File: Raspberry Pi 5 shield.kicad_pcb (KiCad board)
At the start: 2 copper layers, 65 x 56 mm, 18 parts, among them J1 Raspberry Connector, J2 Conn_02x02_Odd_Even, U1 MCP2515-xSO

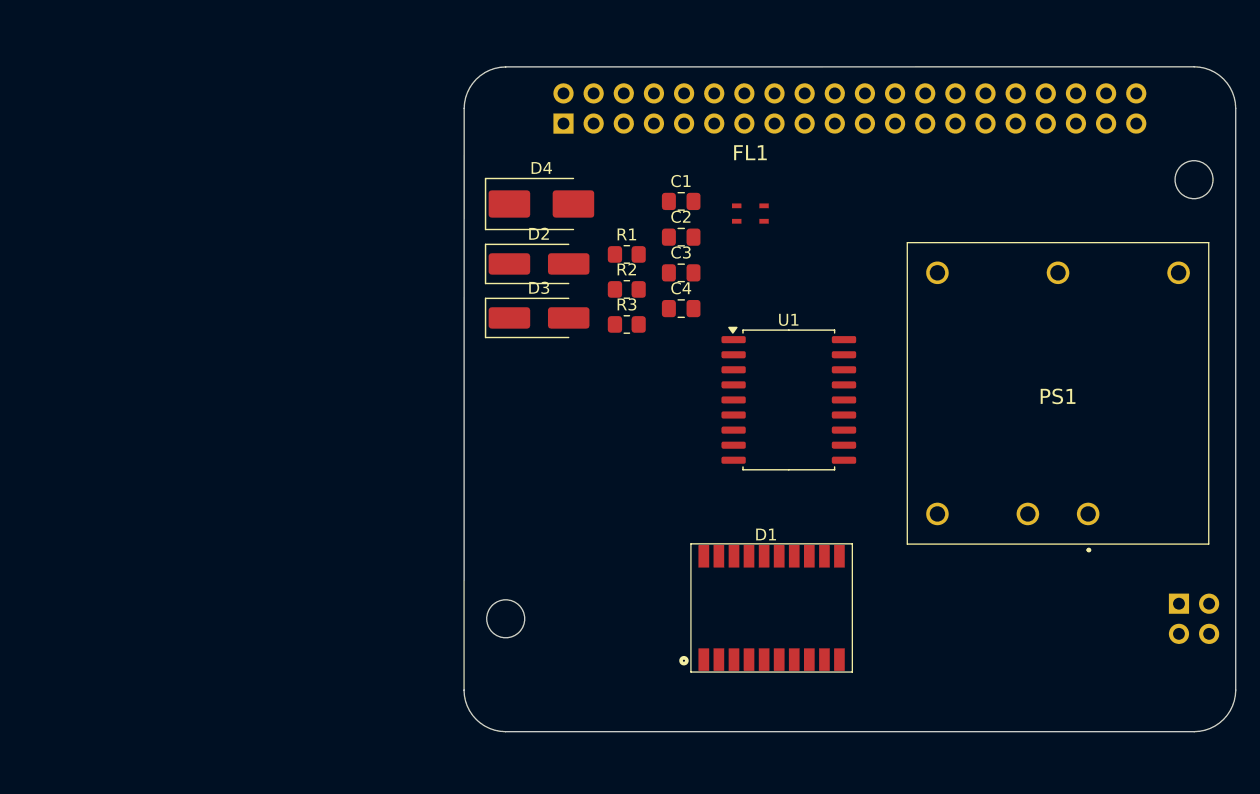
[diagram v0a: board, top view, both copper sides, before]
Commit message: Добавил конденсаторы по выходу
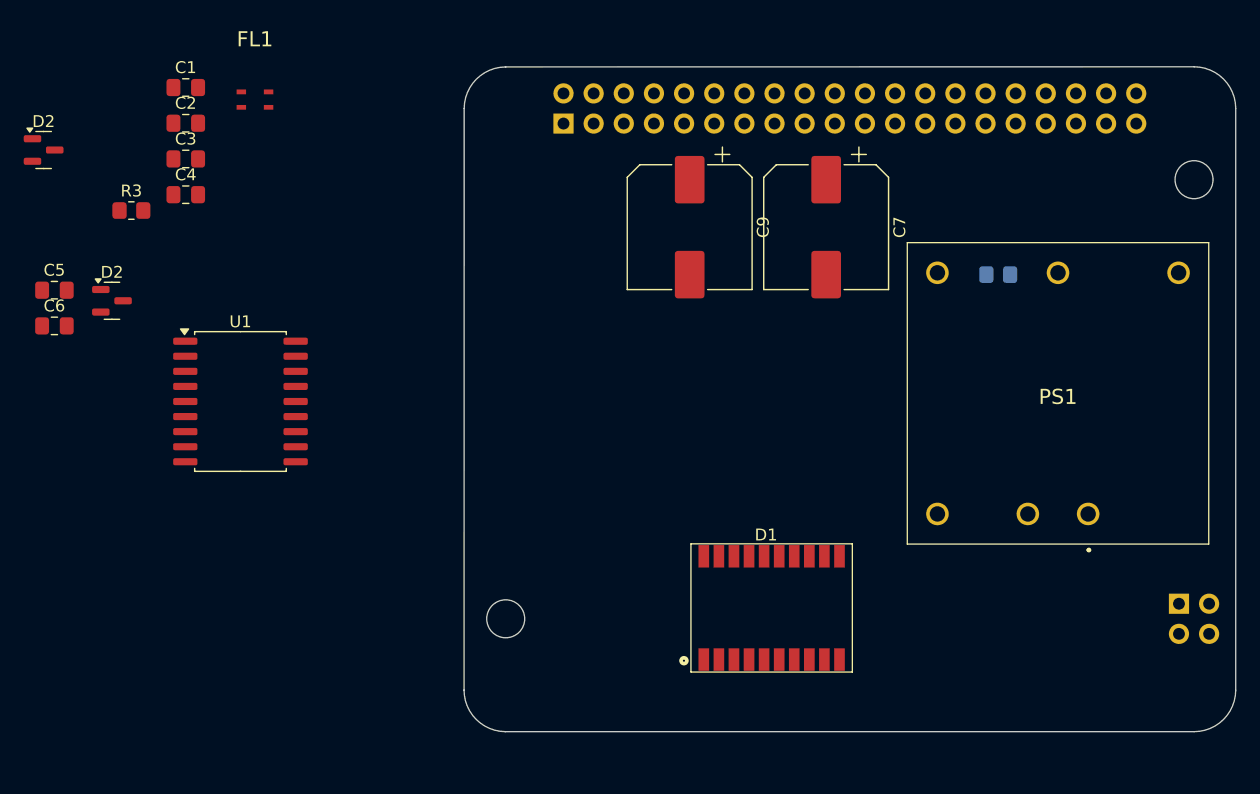
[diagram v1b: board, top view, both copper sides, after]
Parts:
- removed D3: 1N4007, Diode_SMD:D_SMA_Handsoldering
- removed D4: SMBJ30CA, Diode_SMD:D_SMB_Handsoldering
- removed R1, R2: 0, Resistor_SMD:R_0805_2012Metric_Pad1.20x1.40mm_HandSolder
- added C5: 0.1u, Capacitor_SMD:C_0805_2012Metric_Pad1.18x1.45mm_HandSolder, F.Cu at (69.6, 84.8)
- added C6: 0.1u, Capacitor_SMD:C_0805_2012Metric_Pad1.18x1.45mm_HandSolder, F.Cu at (69.6, 87.9)
- added C7: 470u, Capacitor_SMD:CP_Elec_10x10, F.Cu at (134.6, 79.5)
- added C9: 470u, Capacitor_SMD:CP_Elec_10x10, F.Cu at (123.1, 79.5)
- added D2: PESD2CAN, Package_TO_SOT_SMD:SOT-23, F.Cu at (74.5, 85.7)
- added R4: 15k, Resistor_SMD:R_0805_2012Metric_Pad1.20x1.40mm_HandSolder, B.Cu at (149.1, 83.5)
- D2: value 1N4007 -> PESD2CAN; footprint Diode_SMD:D_SMA_Handsoldering -> Package_TO_SOT_SMD:SOT-23
- moved U1 46.2 mm to (85.3, 94.2)
- moved FL1 42.8 mm to (86.5, 68.8)
- moved C1 42.8 mm to (80.7, 67.8)
- moved C2 42.8 mm to (80.7, 70.8)
- moved C3 42.8 mm to (80.7, 73.8)
- moved C4 42.8 mm to (80.7, 76.8)
- moved D2 42.8 mm to (68.7, 73.0)
- moved R3 42.8 mm to (76.1, 78.1)
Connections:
- D2 pad 1: Net-(D2-K) -> CANL
- D2 pad 2: Net-(D2-A) -> CANH
- FL1 pad 2: Net-(D2-A) -> CANH
- FL1 pad 4: Net-(D4-A1) -> CANL
- PS1 pad 3: unconnected-(PS1-+VOUT-Pad3) -> +5V
- PS1 pad 4: unconnected-(PS1-TRIM-Pad4) -> Net-(PS1-TRIM)
- PS1 pad 5: unconnected-(PS1--VOUT-Pad5) -> GND

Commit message: Добавил индикацию
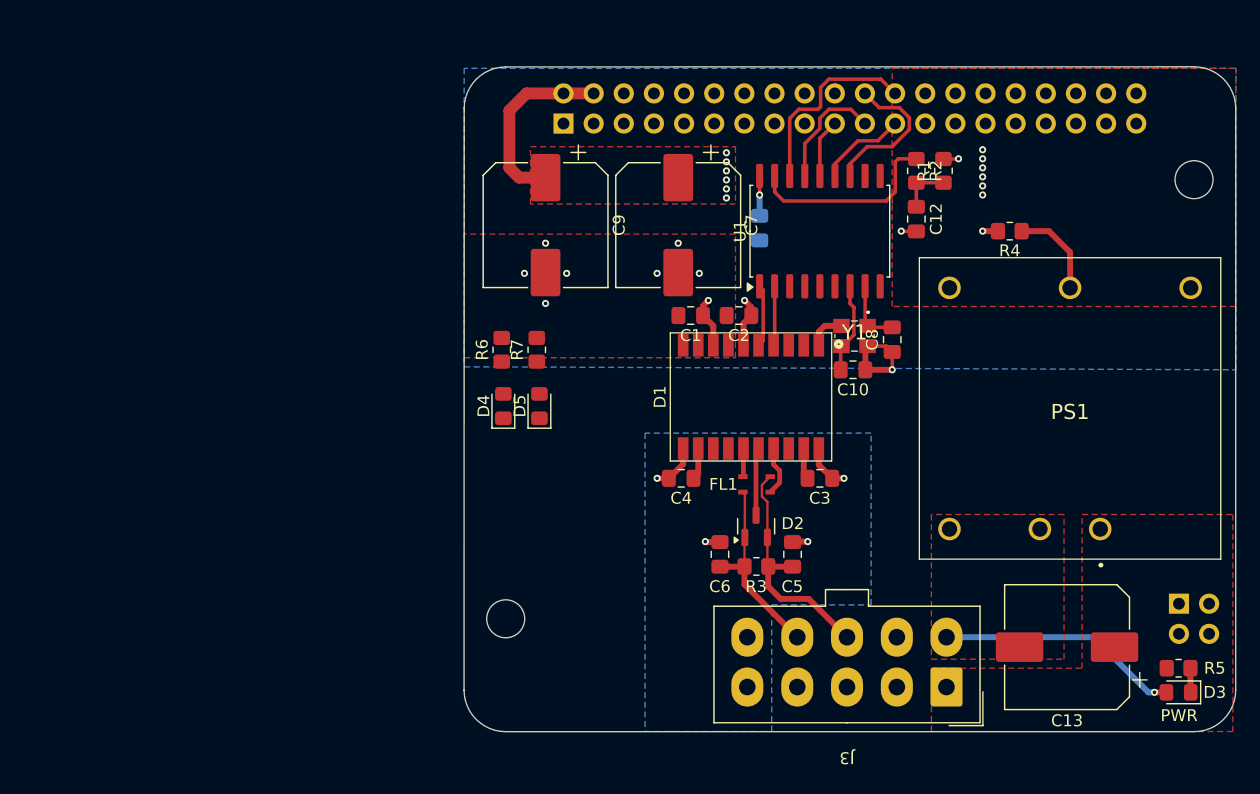
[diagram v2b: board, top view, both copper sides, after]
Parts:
- removed the D2 at (74.5, 85.7)
- removed the D2 at (68.7, 73.0)
- added C10: 22p, Capacitor_SMD:C_0805_2012Metric_Pad1.18x1.45mm_HandSolder, F.Cu at (136.9, 91.6)
- added C11: 1u, Capacitor_SMD:C_0805_2012Metric_Pad1.18x1.45mm_HandSolder, B.Cu at (129.0, 79.6)
- added C12: 0.1u, Capacitor_SMD:C_0805_2012Metric_Pad1.18x1.45mm_HandSolder, F.Cu at (142.2, 78.9)
- added C13: 100u, Capacitor_SMD:CP_Elec_10x10, F.Cu at (154.9, 114.9)
- added C8: 22p, Capacitor_SMD:C_0805_2012Metric_Pad1.18x1.45mm_HandSolder, F.Cu at (140.2, 89.0)
- added D2: PESD2CAN, Package_TO_SOT_SMD:SOT-23, F.Cu at (128.7, 104.7)
- added D3: PWR, LED_SMD:LED_0805_2012Metric_Pad1.15x1.40mm_HandSolder, F.Cu at (164.3, 118.7)
- added D4: LED_Small, LED_SMD:LED_0805_2012Metric_Pad1.15x1.40mm_HandSolder, F.Cu at (107.4, 94.6)
- added D5: LED_Small, LED_SMD:LED_0805_2012Metric_Pad1.15x1.40mm_HandSolder, F.Cu at (110.5, 94.6)
- added J3: DS1073-01-2x5-MR3T6, Molex_My:MIni-Fit_02x05_Vertical, F.Cu at (136.4, 116.6)
- added R1: 1k, Resistor_SMD:R_0805_2012Metric_Pad1.20x1.40mm_HandSolder, F.Cu at (144.5, 74.8)
- added R2: 1k, Resistor_SMD:R_0805_2012Metric_Pad1.20x1.40mm_HandSolder, F.Cu at (142.2, 74.8)
- added R5: 3k, Resistor_SMD:R_0805_2012Metric_Pad1.20x1.40mm_HandSolder, F.Cu at (164.3, 116.7)
- added R6: 3k, Resistor_SMD:R_0805_2012Metric_Pad1.20x1.40mm_HandSolder, F.Cu at (107.3, 89.9)
- added R7: 3k, Resistor_SMD:R_0805_2012Metric_Pad1.20x1.40mm_HandSolder, F.Cu at (110.3, 89.9)
- added Y1: X322516MOB4SI, Crystal_My:X322516MOB4SI, F.Cu at (137.0, 88.7)
- R4: moved to F.Cu
- moved C5 66.1 mm to (131.8, 107.1), turned to -90 degrees
- moved R3 60.6 mm to (128.8, 108.1)
- moved C3 59.8 mm to (134.1, 100.7), turned to 180 degrees
- moved C6 59.3 mm to (125.7, 107.1), turned to 90 degrees
- moved FL1 53.3 mm to (128.8, 101.2), turned to 180 degrees
- moved U1 50.9 mm to (134.1, 79.9), turned to 90 degrees
- moved C2 49.3 mm to (127.3, 87.0), turned to 180 degrees
- moved C4 48.1 mm to (122.4, 100.7), turned to 180 degrees
- moved C1 46.7 mm to (123.2, 87.0), turned to 180 degrees
- moved D1 17.9 mm to (128.3, 93.8), turned to 180 degrees
- moved C7 12.5 mm to (122.2, 79.4)
- moved C9 12.1 mm to (111.0, 79.4)
- moved R4 3.79 mm to (150.1, 79.9)
- moved PS1 1.63 mm to (157.7, 105.0)
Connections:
- C3 pad 1: GNDPWR -> GND_CAN
- C4 pad 2: GNDPWR -> GND_CAN
- C5 pad 1: GNDPWR -> GND_CAN
- C6 pad 2: GNDPWR -> GND_CAN
- D1 pad 11: GNDPWR -> GND_CAN
- D1 pad 13: GNDPWR -> GND_CAN
- D1 pad 16: GNDPWR -> GND_CAN
- D1 pad 18: GNDPWR -> GND_CAN
- D1 pad 20: GNDPWR -> GND_CAN
- J1 pad 11: unconnected-(J1-Pin_11-Pad11) -> GPIO_17
- J1 pad 12: unconnected-(J1-Pin_12-Pad12) -> GPIO_18
- J1 pad 13: unconnected-(J1-Pin_13-Pad13) -> GPIO_27
- J1 pad 15: unconnected-(J1-Pin_15-Pad15) -> GPIO_22
- J1 pad 16: unconnected-(J1-Pin_16-Pad16) -> GPIO_23
- J1 pad 18: unconnected-(J1-Pin_18-Pad18) -> GPIO_24
- J1 pad 22: unconnected-(J1-Pin_22-Pad22) -> ~{INT}
- J1 pad 24: unconnected-(J1-Pin_24-Pad24) -> CE0
- J1 pad 26: unconnected-(J1-Pin_26-Pad26) -> CE1
- J1 pad 29: unconnected-(J1-Pin_29-Pad29) -> GPIO_5
- J1 pad 31: unconnected-(J1-Pin_31-Pad31) -> GPIO_6
- J1 pad 32: unconnected-(J1-Pin_32-Pad32) -> GPIO_12
- J1 pad 33: unconnected-(J1-Pin_33-Pad33) -> GPIO_13
- J1 pad 35: unconnected-(J1-Pin_35-Pad35) -> GPIO_19
- J1 pad 36: unconnected-(J1-Pin_36-Pad36) -> GPIO_16
- J1 pad 37: unconnected-(J1-Pin_37-Pad37) -> GPIO_26
- J1 pad 38: unconnected-(J1-Pin_38-Pad38) -> GPIO_20
- J1 pad 40: unconnected-(J1-Pin_40-Pad40) -> GPIO_21
- PS1 pad 1: unconnected-(PS1-+VIN-Pad1) -> GNDPWR
- PS1 pad 2: unconnected-(PS1--VIN-Pad2) -> +24V
- U1 pad 12: unconnected-(U1-~{INT}-Pad12) -> ~{INT}
- U1 pad 13: unconnected-(U1-SCK-Pad13) -> SPI_SCLK
- U1 pad 14: unconnected-(U1-SI-Pad14) -> SPI_MOSI
- U1 pad 15: unconnected-(U1-SO-Pad15) -> SPI_MISO
- U1 pad 16: unconnected-(U1-~{CS}-Pad16) -> CE0
- U1 pad 17: unconnected-(U1-~{RESET}-Pad17) -> Net-(U1-~{RESET})
- U1 pad 7: unconnected-(U1-OSC2-Pad7) -> Net-(U1-OSC2)
- U1 pad 8: unconnected-(U1-OSC1-Pad8) -> Net-(U1-OSC1)
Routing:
- net +24V: track 0.00 -> 20.5 mm, vias 0 -> 1
- net +5V: track 0.00 -> 20.2 mm, vias 0 -> 13
- net CANH: track 0.00 -> 20.2 mm
- net Net-(U1-~{RESET}): track 0.00 -> 16.9 mm
- net CE0: track 0.00 -> 16.6 mm
- net GND_CAN: track 0.00 -> 16.3 mm, vias 0 -> 4
- net CANL: track 0.00 -> 16.2 mm
- net GND: track 0.00 -> 14.5 mm, vias 0 -> 10
- net ~{INT}: track 0.00 -> 12.8 mm
- net SPI_MISO: track 0.00 -> 9.99 mm
- net +3.3V: track 0.00 -> 8.92 mm, vias 0 -> 3
- net Net-(U1-OSC2): track 0.00 -> 7.95 mm
- net Net-(PS1-TRIM): track 0.00 -> 7.82 mm
- net SPI_SCLK: track 0.00 -> 7.50 mm
- net Net-(U1-OSC1): track 0.00 -> 5.82 mm
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- added copper zone on F.Cu, net +24V
- added copper zone on In2.Cu, net +3.3V
- added copper zone on F.Cu, net +5V
- added copper zone on In1.Cu, net +5V
- added copper zone on B.Cu, net GND
- added copper zone on F.Cu, net GND
- added copper zone on F.Cu, net GNDPWR
- added copper zone on B.Cu, net GND_CAN
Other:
- copper layers 2 -> 4
- board text added: "PWR"

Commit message: Добавил BOM
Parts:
- moved R7 0.23 mm to (110.5, 89.9)
- moved R6 0.13 mm to (107.4, 89.9)
- turned D4 to -90 degrees
- turned D5 to -90 degrees
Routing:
- net +5V: track 20.2 -> 75.3 mm, vias 13 -> 16
- net +3.3V: track 8.92 -> 39.1 mm, vias 3 -> 4
- net Net-(D5-K): track 0.00 -> 2.72 mm
- net Net-(D4-K): track 0.00 -> 2.72 mm
- net GND: track 14.5 -> 17.1 mm, vias 10 -> 12
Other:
- board text added: "3.3V"
- board text added: "5V"

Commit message: Исправил косяки в схеме
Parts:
- J3: value DS1073-01-2x5-MR3T6 -> DS1073-01-2x5-MVT6
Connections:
- C13 pad 1: GNDPWR -> +24V
- C13 pad 2: +24V -> GNDPWR
- J3 pad 1: GNDPWR -> +24V
- J3 pad 6: +24V -> GNDPWR
- PS1 pad 1: GNDPWR -> +24V
- PS1 pad 2: +24V -> GNDPWR
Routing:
- net GNDPWR: track 0.00 -> 19.6 mm, vias 0 -> 1
- net Net-(D1-Visoin): track 5.31 -> 17.5 mm, vias 0 -> 2
- net GND: track 17.1 -> 22.8 mm
- net +24V: track 20.5 -> 18.7 mm
- added copper zone on F.Cu, net GND_CAN
